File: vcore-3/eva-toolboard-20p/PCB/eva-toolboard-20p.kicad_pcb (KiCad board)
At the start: 2 copper layers, 44.1 x 48.8 mm, 12 parts, among them J1 TH0, J2 HEATER, J3 STEPPER, J4 Main connector, J5 HEFAN, J6 PFAN1, J7 PFAN2, J8 E_X, J9 PROBE

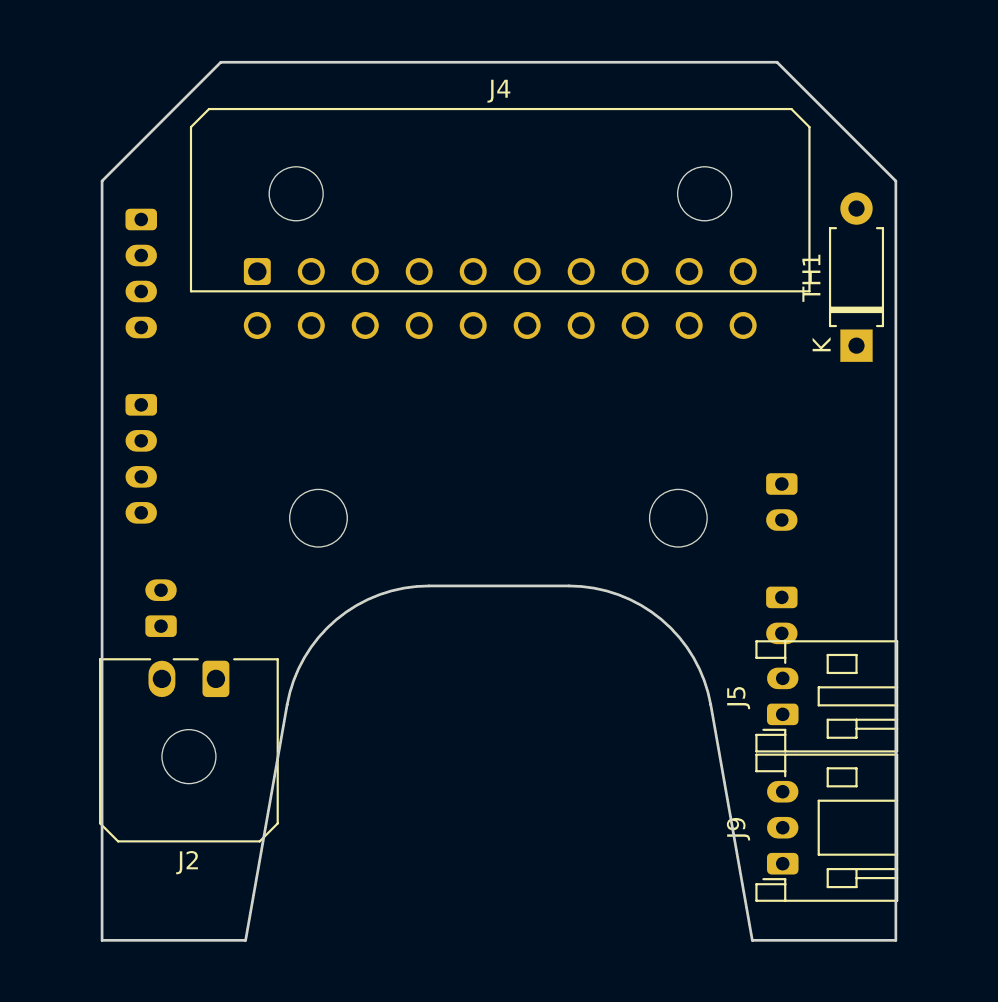
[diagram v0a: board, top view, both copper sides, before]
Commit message: Routed PCB and adapted schematic
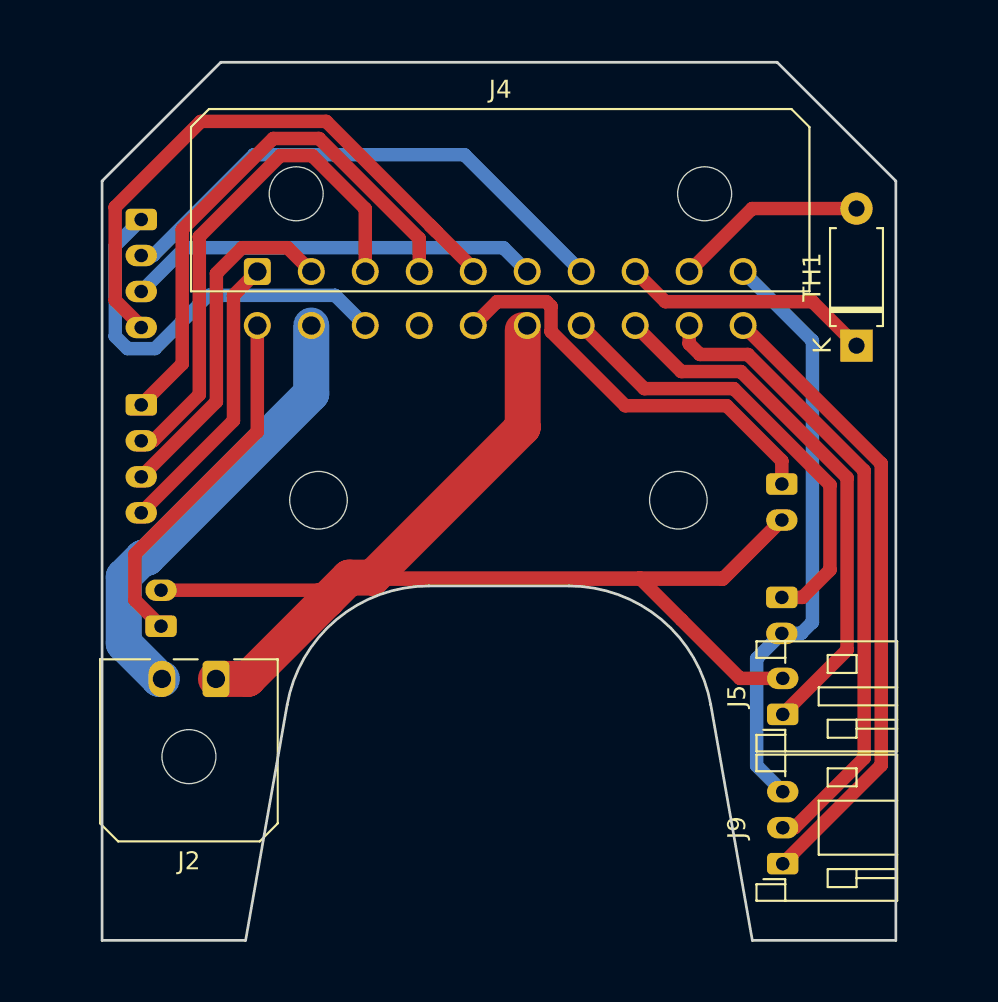
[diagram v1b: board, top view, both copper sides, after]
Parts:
- J5: value HEFAN -> HOTENDFAN
- J6: value PFAN1 -> PARTFAN_1
- J7: value PFAN2 -> PARTFAN_2
- J8: value E_X -> ENDSTOP_X
- moved L 1.00 mm to (141.5, 100.5)
- moved R 1.00 mm to (161.5, 100.5)
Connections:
- J3 pad 1: Net-(J3-Pad1) -> Net-(J4-Pad13)
- J4 pad 11: +24V -> Net-(J7-Pad1)
- J4 pad 14: Net-(J4-Pad14) -> unconnected-(J4-Pad14)
- J4 pad 16: Net-(J4-Pad16) -> +24V
- J4 pad 19: unconnected-(J4-Pad19) -> Net-(J4-Pad19)
- J4 pad 8: Net-(J3-Pad1) -> Net-(J4-Pad8)
- J6 pad 1: Net-(J4-Pad17) -> Net-(J4-Pad15)
- J7 pad 1: Net-(J4-Pad16) -> Net-(J7-Pad1)
- J8 pad 1: Net-(J4-Pad15) -> Net-(J4-Pad17)
- J9 pad 2: Net-(J4-Pad14) -> Net-(J4-Pad19)
- TH1 pad 1: Net-(J4-Pad13) -> Net-(J4-Pad8)
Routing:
- net +24V: track 0.00 -> 96.2 mm
- net Net-(J4-Pad19): track 0.00 -> 35.8 mm
- net +5V: track 0.00 -> 35.4 mm
- net Net-(J3-Pad4): track 0.00 -> 33.3 mm
- net GND: track 0.00 -> 33.0 mm
- net Net-(J1-Pad1): track 0.00 -> 30.1 mm
- net Net-(J4-Pad18): track 0.00 -> 29.9 mm
- net Net-(J3-Pad2): track 0.00 -> 29.5 mm
- net Net-(J1-Pad2): track 0.00 -> 28.9 mm
- net Net-(J4-Pad17): track 0.00 -> 25.5 mm
- net Net-(J2-Pad2): track 0.00 -> 25.1 mm
- net Net-(J4-Pad15): track 0.00 -> 23.5 mm
- net Net-(J4-Pad13): track 0.00 -> 23.2 mm
- net Net-(J3-Pad3): track 0.00 -> 23.0 mm
- net Net-(J7-Pad1): track 0.00 -> 20.1 mm
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
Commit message: Latest pcb update
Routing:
- net GND: track 33.0 -> 0.00 mm, vias 0 -> 6
- added copper zone on B.Cu, net GND
- added copper zone on F.Cu, net GND
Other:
- board text added: "Loveboard 1.0"
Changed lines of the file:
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@@
   (gr_line (start 133.475 106.76) (end 133.475 107.06) (layer "User.2") (width 0.15))
   (gr_line (start 135.475 103.96) (end 135.475 104.46) (layer "User.2") (width 0.15))
+  (gr_text "Loveboard 1.0" (at 151.5 97.2) (layer "F.SilkS")
+    (effects (font (size 1.5 1.5) (thickness 0.3)))
+  )
   (segment (start 141.53331 80.395959) (end 147.1 85.962649) (width 0.75) (layer "F.Cu") (net 1))
   (segment (start 138.98669 80.395959) (end 141.53331 80.395959) (width 0.75) (layer "F.Cu") (net 1))
@@
   (segment (start 165.6 84.29) (end 162.1 87.79) (width 0.75) (layer "F.Cu") (net 10))
   (segment (start 171.4 84.29) (end 165.6 84.29) (width 0.75) (layer "F.Cu") (net 10))
-  (segment (start 168.325 107.9) (end 168.95 107.275) (width 0.75) (layer "B.Cu") (net 11))
-  (segment (start 168.95 91.64) (end 165.1 87.79) (width 0.75) (layer "B.Cu") (net 11))
-  (segment (start 165.85048 109.29952) (end 167.25 107.9) (width 0.75) (layer "B.Cu") (net 11))
-  (segment (start 167.25 107.9) (end 168.325 107.9) (width 0.75) (layer "B.Cu") (net 11))
-  (segment (start 165.85048 115.25048) (end 165.85048 109.29952) (width 0.75) (layer "B.Cu") (net 11))
-  (segment (start 168.95 107.275) (end 168.95 91.64) (width 0.75) (layer "B.Cu") (net 11))
-  (segment (start 167.3 116.7) (end 165.85048 115.25048) (width 0.75) (layer "B.Cu") (net 11))
+  (via (at 135.1 81.4) (size 0.8) (drill 0.4) (layers "F.Cu" "B.Cu") (free) (net 11))
+  (via (at 137 113) (size 0.8) (drill 0.4) (layers "F.Cu" "B.Cu") (free) (net 11))
+  (via (at 131.1 93.2) (size 0.8) (drill 0.4) (layers "F.Cu" "B.Cu") (free) (net 11))
+  (via (at 156 96) (size 0.8) (drill 0.4) (layers "F.Cu" "B.Cu") (free) (net 11))
+  (via (at 147 96) (size 0.8) (drill 0.4) (layers "F.Cu" "B.Cu") (free) (net 11))
+  (via (at 149 83.3) (size 0.8) (drill 0.4) (layers "F.Cu" "B.Cu") (free) (net 11))
   (segment (start 142.424511 89.114511) (end 144.1 90.79) (width 0.75) (layer "B.Cu") (net 12))
   (segment (start 131.65 84.9) (end 130.20048 86.34952) (width 0.75) (layer "B.Cu") (net 12))
@@
   (segment (start 168.955489 89.465489) (end 160.775489 89.465489) (width 0.75) (layer "F.Cu") (net 20))
   (segment (start 160.775489 89.465489) (end 159.1 87.79) (width 0.75) (layer "F.Cu") (net 20))
+  (zone (net 11) (net_name "GND") (layers F&B.Cu) (hatch edge 0.508)
+    (connect_pads (clearance 0.508))
+    (min_thickness 0.254) (filled_areas_thickness no)
+    (fill yes (thermal_gap 0.508) (thermal_bridge_width 0.508))
+    (polygon
+      (pts
+        (xy 177.25 75.25)
+        (xy 176.6 126.4)
+        (xy 125.8 126.35)
+        (xy 125.8 74.7)
+      )
+    )
+  )
   (group "" (id a74a2ecb-b3d3-4857-b4a0-0f6b8b1ff3de)
     (members
